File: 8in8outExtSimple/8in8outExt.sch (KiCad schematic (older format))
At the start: 70 parts, among them P1 CONN_10X2, Q1 PNP, Q10 NPN, Q11 NPN, Q12 NPN, Q13 NPN, Q14 NPN, Q15 NPN, Q16 NPN, Q2 PNP, Q3 PNP, Q4 PNP, Q5 PNP, Q6 PNP, Q7 PNP, Q8 PNP, Q9 NPN

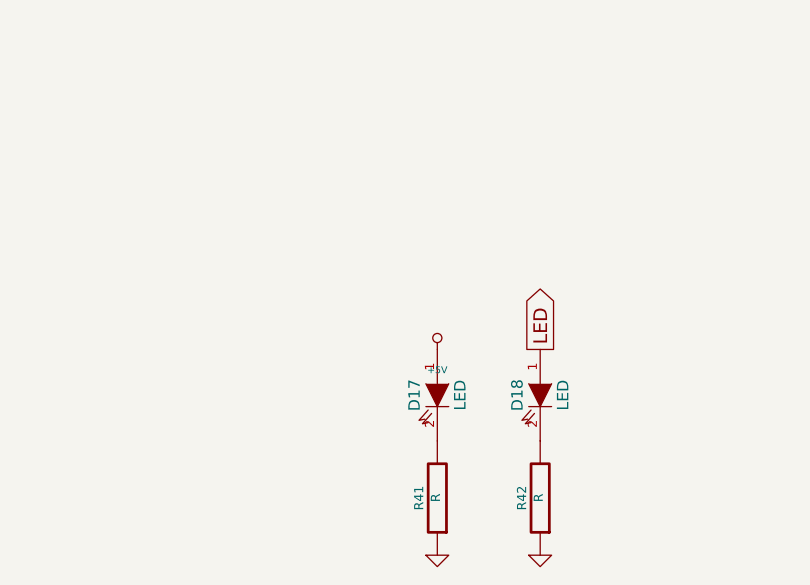
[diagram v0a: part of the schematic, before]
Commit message: agrandissement taille du panneau ajout NPN pour commande led status serigraphie
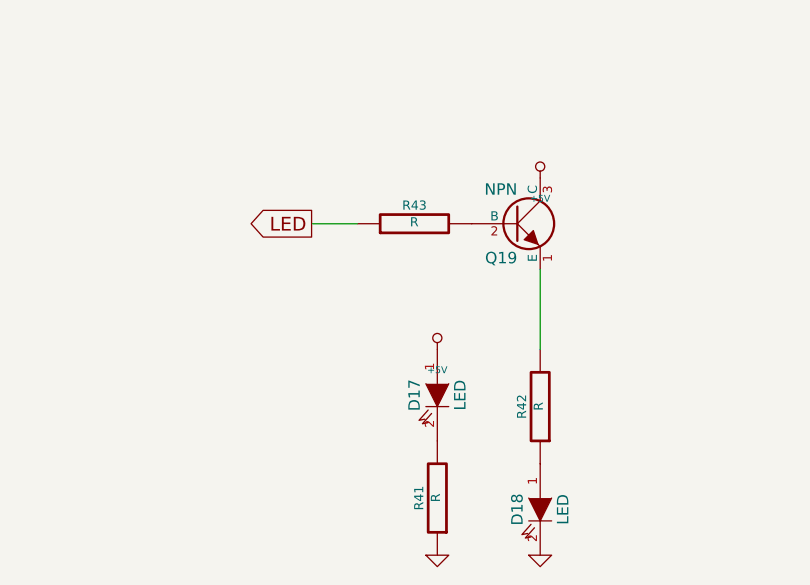
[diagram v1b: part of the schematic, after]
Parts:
- added Q19: NPN, symbol NPN
- added R43: R, symbol R
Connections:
- net +5V: now also Q19.3 (C)
- net GND: now also D18.2 (K); no longer R42.1
- net LED: now also R43.1; no longer D18.1 (A)
- net at R42.2: now also Q19.1 (E); no longer D18.2 (K)
- new net: D18.1 (A), R42.1
- new net: Q19.2 (B), R43.2
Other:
- moved on the sheet: D18, R42
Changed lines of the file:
@@
 L LED D18
 U 1 1 51739912
-P 12700 6750
-F 0 "D18" H 12700 6650 50  0000 C CNN
-F 1 "LED" H 12700 6850 50  0000 C CNN
-F 2 "~" H 12700 6750 60  0000 C CNN
-F 3 "~" H 12700 6750 60  0000 C CNN
-	1    12700 6750
+P 12700 7250
+F 0 "D18" H 12700 7150 50  0000 C CNN
+F 1 "LED" H 12700 7350 50  0000 C CNN
+F 2 "~" H 12700 7250 60  0000 C CNN
+F 3 "~" H 12700 7250 60  0000 C CNN
+	1    12700 7250
 	0    1    1    0
 $EndComp
@@
 L R R42
 U 1 1 51739918
-P 12700 7200
-F 0 "R42" V 12780 7200 40  0000 C CNN
-F 1 "R" V 12707 7199 40  0000 C CNN
-F 2 "~" V 12630 7200 30  0000 C CNN
-F 3 "~" H 12700 7200 30  0000 C CNN
-	1    12700 7200
+P 12700 6800
+F 0 "R42" V 12780 6800 40  0000 C CNN
+F 1 "R" V 12707 6799 40  0000 C CNN
+F 2 "~" V 12630 6800 30  0000 C CNN
+F 3 "~" H 12700 6800 30  0000 C CNN
+	1    12700 6800
 	-1   0    0    1
 $EndComp
@@
 	1    0    0    -1
 $EndComp
-Text GLabel 12700 6550 1    60   Output ~ 0
+Text GLabel 11700 6000 0    60   Output ~ 0
 LED
 $Comp
-L +5V #PWR015
+L +5V #PWR07
 U 1 1 51766852
 P 6200 800
-F 0 "#PWR015" H 6200 710 20  0001 C CNN
+F 0 "#PWR07" H 6200 710 20  0001 C CNN
 F 1 "+5V" H 6200 710 30  0000 C CNN
 F 2 "" H 6200 800 60  0000 C CNN
@@
 RESET
 $Comp
-L GND #PWR016
+L GND #PWR08
 U 1 1 517986C9
 P 14250 6800
-F 0 "#PWR016" H 14250 6800 30  0001 C CNN
+F 0 "#PWR08" H 14250 6800 30  0001 C CNN
 F 1 "GND" H 14250 6870 30  0001 C CNN
 F 2 "" H 14250 6800 60  0000 C CNN
@@
 $EndComp
 $Comp
-L GND #PWR017
+L GND #PWR09
 U 1 1 522CC8B0
 P 7150 2000
-F 0 "#PWR017" H 7150 2000 30  0001 C CNN
+F 0 "#PWR09" H 7150 2000 30  0001 C CNN
 F 1 "GND" H 7150 2070 30  0001 C CNN
 F 2 "" H 7150 2000 60  0000 C CNN
@@
 $EndComp
 $Comp
-L +5V #PWR018
+L +5V #PWR010
 U 1 1 522CC8B6
 P 6200 1450
-F 0 "#PWR018" H 6200 1360 20  0001 C CNN
+F 0 "#PWR010" H 6200 1360 20  0001 C CNN
 F 1 "+5V" H 6200 1360 30  0000 C CNN
 F 2 "" H 6200 1450 60  0000 C CNN
@@
 $EndComp
 $Comp
-L GND #PWR019
+L GND #PWR011
 U 1 1 522CC8D7
 P 7150 2650
-F 0 "#PWR019" H 7150 2650 30  0001 C CNN
+F 0 "#PWR011" H 7150 2650 30  0001 C CNN
 F 1 "GND" H 7150 2720 30  0001 C CNN
 F 2 "" H 7150 2650 60  0000 C CNN
@@
 $EndComp
 $Comp
-L +5V #PWR020
+L +5V #PWR012
 U 1 1 522CC8DD
 P 6200 2100
-F 0 "#PWR020" H 6200 2010 20  0001 C CNN
+F 0 "#PWR012" H 6200 2010 20  0001 C CNN
 F 1 "+5V" H 6200 2010 30  0000 C CNN
 F 2 "" H 6200 2100 60  0000 C CNN
@@
 $EndComp
 $Comp
-L GND #PWR021
+L GND #PWR013
 U 1 1 522CC908
 P 7150 3300
-F 0 "#PWR021" H 7150 3300 30  0001 C CNN
+F 0 "#PWR013" H 7150 3300 30  0001 C CNN
 F 1 "GND" H 7150 3370 30  0001 C CNN
 F 2 "" H 7150 3300 60  0000 C CNN
@@
 $EndComp
 $Comp
-L +5V #PWR022
+L +5V #PWR014
 U 1 1 522CC90E
 P 6200 2750
-F 0 "#PWR022" H 6200 2660 20  0001 C CNN
+F 0 "#PWR014" H 6200 2660 20  0001 C CNN
 F 1 "+5V" H 6200 2660 30  0000 C CNN
 F 2 "" H 6200 2750 60  0000 C CNN
@@
 $EndComp
 $Comp
-L GND #PWR023
+L GND #PWR015
 U 1 1 522CC930
 P 7150 4000
-F 0 "#PWR023" H 7150 4000 30  0001 C CNN
+F 0 "#PWR015" H 7150 4000 30  0001 C CNN
 F 1 "GND" H 7150 4070 30  0001 C CNN
 F 2 "" H 7150 4000 60  0000 C CNN
@@
 $EndComp
 $Comp
-L +5V #PWR024
+L +5V #PWR016
 U 1 1 522CC936
 P 6200 3450
-F 0 "#PWR024" H 6200 3360 20  0001 C CNN
+F 0 "#PWR016" H 6200 3360 20  0001 C CNN
 F 1 "+5V" H 6200 3360 30  0000 C CNN
 F 2 "" H 6200 3450 60  0000 C CNN
@@
 $EndComp
 $Comp
-L GND #PWR025
+L GND #PWR017
 U 1 1 522CC957
 P 7150 4650
-F 0 "#PWR025" H 7150 4650 30  0001 C CNN
+F 0 "#PWR017" H 7150 4650 30  0001 C CNN
 F 1 "GND" H 7150 4720 30  0001 C CNN
 F 2 "" H 7150 4650 60  0000 C CNN
@@
 $EndComp
 $Comp
-L +5V #PWR026
+L +5V #PWR018
 U 1 1 522CC95D
 P 6200 4100
-F 0 "#PWR026" H 6200 4010 20  0001 C CNN
+F 0 "#PWR018" H 6200 4010 20  0001 C CNN
 F 1 "+5V" H 6200 4010 30  0000 C CNN
 F 2 "" H 6200 4100 60  0000 C CNN
@@
 $EndComp
 $Comp
-L GND #PWR027
+L GND #PWR019
 U 1 1 522CC97E
 P 7150 5300
-F 0 "#PWR027" H 7150 5300 30  0001 C CNN
+F 0 "#PWR019" H 7150 5300 30  0001 C CNN
 F 1 "GND" H 7150 5370 30  0001 C CNN
 F 2 "" H 7150 5300 60  0000 C CNN
@@
 $EndComp
 $Comp
-L +5V #PWR028
+L +5V #PWR020
 U 1 1 522CC984
 P 6200 4750
-F 0 "#PWR028" H 6200 4660 20  0001 C CNN
+F 0 "#PWR020" H 6200 4660 20  0001 C CNN
 F 1 "+5V" H 6200 4660 30  0000 C CNN
 F 2 "" H 6200 4750 60  0000 C CNN
@@
 $EndComp
 $Comp
-L GND #PWR029
+L GND #PWR021
 U 1 1 522CC9A5
 P 7150 5950
-F 0 "#PWR029" H 7150 5950 30  0001 C CNN
+F 0 "#PWR021" H 7150 5950 30  0001 C CNN
 F 1 "GND" H 7150 6020 30  0001 C CNN
 F 2 "" H 7150 5950 60  0000 C CNN
@@
 $EndComp
 $Comp
-L +5V #PWR030
+L +5V #PWR022
 U 1 1 522CC9AB
 P 6200 5400
-F 0 "#PWR030" H 6200 5310 20  0001 C CNN
+F 0 "#PWR022" H 6200 5310 20  0001 C CNN
 F 1 "+5V" H 6200 5310 30  0000 C CNN
 F 2 "" H 6200 5400 60  0000 C CNN
@@
 $EndComp
 $Comp
-L GND #PWR031
+L GND #PWR023
 U 1 1 522CC9E4
 P 9800 1350
-F 0 "#PWR031" H 9800 1350 30  0001 C CNN
+F 0 "#PWR023" H 9800 1350 30  0001 C CNN
 F 1 "GND" H 9800 1420 30  0001 C CNN
 F 2 "" H 9800 1350 60  0000 C CNN
@@
 $EndComp
 $Comp
-L +5V #PWR032
+L +5V #PWR024
 U 1 1 522CC9EA
 P 8850 800
-F 0 "#PWR032" H 8850 710 20  0001 C CNN
+F 0 "#PWR024" H 8850 710 20  0001 C CNN
 F 1 "+5V" H 8850 710 30  0000 C CNN
 F 2 "" H 8850 800 60  0000 C CNN
@@
 $EndComp
 $Comp
-L GND #PWR033
+L GND #PWR025
 U 1 1 522CCA2C
 P 9800 2000
-F 0 "#PWR033" H 9800 2000 30  0001 C CNN
+F 0 "#PWR025" H 9800 2000 30  0001 C CNN
 F 1 "GND" H 9800 2070 30  0001 C CNN
 F 2 "" H 9800 2000 60  0000 C CNN
@@
 $EndComp
 $Comp
-L +5V #PWR034
+L +5V #PWR026
 U 1 1 522CCA32
 P 8850 1450
-F 0 "#PWR034" H 8850 1360 20  0001 C CNN
+F 0 "#PWR026" H 8850 1360 20  0001 C CNN
 F 1 "+5V" H 8850 1360 30  0000 C CNN
 F 2 "" H 8850 1450 60  0000 C CNN
@@
 $EndComp
 $Comp
-L GND #PWR035
+L GND #PWR027
 U 1 1 522CCA53
 P 9800 2650
-F 0 "#PWR035" H 9800 2650 30  0001 C CNN
+F 0 "#PWR027" H 9800 2650 30  0001 C CNN
 F 1 "GND" H 9800 2720 30  0001 C CNN
 F 2 "" H 9800 2650 60  0000 C CNN
@@
 $EndComp
 $Comp
-L +5V #PWR036
+L +5V #PWR028
 U 1 1 522CCA59
 P 8850 2100
-F 0 "#PWR036" H 8850 2010 20  0001 C CNN
+F 0 "#PWR028" H 8850 2010 20  0001 C CNN
 F 1 "+5V" H 8850 2010 30  0000 C CNN
 F 2 "" H 8850 2100 60  0000 C CNN
@@
 $EndComp
 $Comp
-L GND #PWR037
+L GND #PWR029
 U 1 1 522CCA7A
 P 9800 3300
-F 0 "#PWR037" H 9800 3300 30  0001 C CNN
+F 0 "#PWR029" H 9800 3300 30  0001 C CNN
 F 1 "GND" H 9800 3370 30  0001 C CNN
 F 2 "" H 9800 3300 60  0000 C CNN
@@
 $EndComp
 $Comp
-L +5V #PWR038
+L +5V #PWR030
 U 1 1 522CCA80
 P 8850 2750
-F 0 "#PWR038" H 8850 2660 20  0001 C CNN
+F 0 "#PWR030" H 8850 2660 20  0001 C CNN
 F 1 "+5V" H 8850 2660 30  0000 C CNN
 F 2 "" H 8850 2750 60  0000 C CNN
@@
 $EndComp
 $Comp
-L GND #PWR039
+L GND #PWR031
 U 1 1 522CCAA1
 P 9800 4000
-F 0 "#PWR039" H 9800 4000 30  0001 C CNN
+F 0 "#PWR031" H 9800 4000 30  0001 C CNN
 F 1 "GND" H 9800 4070 30  0001 C CNN
 F 2 "" H 9800 4000 60  0000 C CNN
@@
 $EndComp
 $Comp
-L +5V #PWR040
+L +5V #PWR032
 U 1 1 522CCAA7
 P 8850 3450
-F 0 "#PWR040" H 8850 3360 20  0001 C CNN
+F 0 "#PWR032" H 8850 3360 20  0001 C CNN
 F 1 "+5V" H 8850 3360 30  0000 C CNN
 F 2 "" H 8850 3450 60  0000 C CNN
@@
 $EndComp
 $Comp
-L GND #PWR041
+L GND #PWR033
 U 1 1 522CCAC8
 P 9850 4650
-F 0 "#PWR041" H 9850 4650 30  0001 C CNN
+F 0 "#PWR033" H 9850 4650 30  0001 C CNN
 F 1 "GND" H 9850 4720 30  0001 C CNN
 F 2 "" H 9850 4650 60  0000 C CNN
@@
 $EndComp
 $Comp
-L +5V #PWR042
+L +5V #PWR034
 U 1 1 522CCACE
 P 8850 4100
-F 0 "#PWR042" H 8850 4010 20  0001 C CNN
+F 0 "#PWR034" H 8850 4010 20  0001 C CNN
 F 1 "+5V" H 8850 4010 30  0000 C CNN
 F 2 "" H 8850 4100 60  0000 C CNN
@@
 $EndComp
 $Comp
-L GND #PWR043
+L GND #PWR035
 U 1 1 522CCAEF
 P 9800 5300
-F 0 "#PWR043" H 9800 5300 30  0001 C CNN
+F 0 "#PWR035" H 9800 5300 30  0001 C CNN
 F 1 "GND" H 9800 5370 30  0001 C CNN
 F 2 "" H 9800 5300 60  0000 C CNN
@@
 $EndComp
 $Comp
-L +5V #PWR044
+L +5V #PWR036
 U 1 1 522CCAF5
 P 8850 4750
-F 0 "#PWR044" H 8850 4660 20  0001 C CNN
+F 0 "#PWR036" H 8850 4660 20  0001 C CNN
 F 1 "+5V" H 8850 4660 30  0000 C CNN
 F 2 "" H 8850 4750 60  0000 C CNN
@@
 $EndComp
 $Comp
-L GND #PWR045
+L GND #PWR037
 U 1 1 522CCB16
 P 9800 5950
-F 0 "#PWR045" H 9800 5950 30  0001 C CNN
+F 0 "#PWR037" H 9800 5950 30  0001 C CNN
 F 1 "GND" H 9800 6020 30  0001 C CNN
 F 2 "" H 9800 5950 60  0000 C CNN
@@
 $EndComp
 $Comp
-L +5V #PWR046
+L +5V #PWR038
 U 1 1 522CCB1C
 P 8850 5400
-F 0 "#PWR046" H 8850 5310 20  0001 C CNN
+F 0 "#PWR038" H 8850 5310 20  0001 C CNN
 F 1 "+5V" H 8850 5310 30  0000 C CNN
 F 2 "" H 8850 5400 60  0000 C CNN
@@
 	1    0    0    -1
 $EndComp
+Wire Wire Line
+	11700 6000 11900 6000
+$Comp
+L +5V #PWR039
+U 1 1 52681A86
+P 12700 5800
+F 0 "#PWR039" H 12700 5710 20  0001 C CNN
+F 1 "+5V" H 12700 5710 30  0000 C CNN
+F 2 "" H 12700 5800 60  0000 C CNN
+F 3 "" H 12700 5800 60  0000 C CNN
+	1    12700 5800
+	1    0    0    -1
+$EndComp
+$Comp
+L R R43
+U 1 1 52681A8C
+P 12150 6000
+F 0 "R43" V 12230 6000 40  0000 C CNN
+F 1 "R" V 12157 6001 40  0000 C CNN
+F 2 "" V 12080 6000 30  0000 C CNN
+F 3 "" H 12150 6000 30  0000 C CNN
+	1    12150 6000
+	0    -1   -1   0
+$EndComp
+$Comp
+L NPN Q19
+U 1 1 52681A92
+P 12600 6000
+F 0 "Q19" H 12600 5850 50  0000 R CNN
+F 1 "NPN" H 12600 6150 50  0000 R CNN
+F 2 "" H 12600 6000 60  0000 C CNN
+F 3 "" H 12600 6000 60  0000 C CNN
+	1    12600 6000
+	1    0    0    -1
+$EndComp
+Wire Wire Line
+	12700 6550 12700 6200
 $EndSCHEMATC

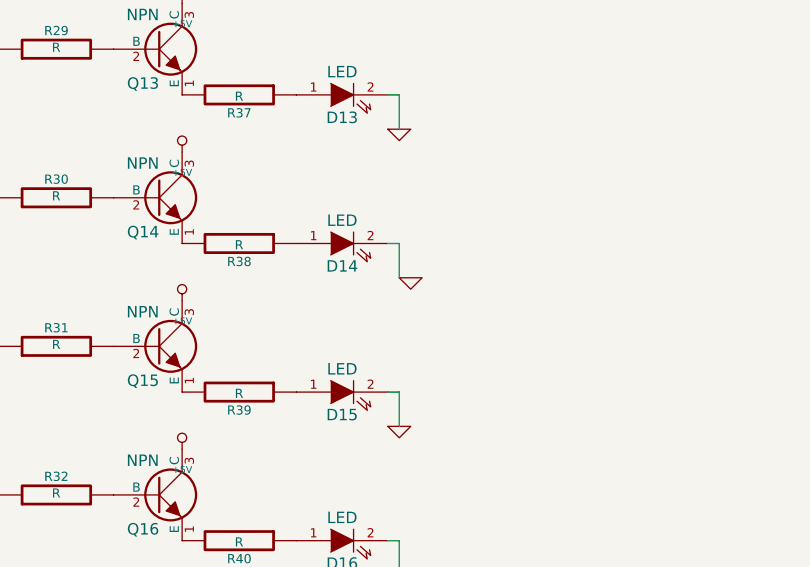
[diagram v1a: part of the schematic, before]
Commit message: correction erreur schema led out5 pas reli? au GND
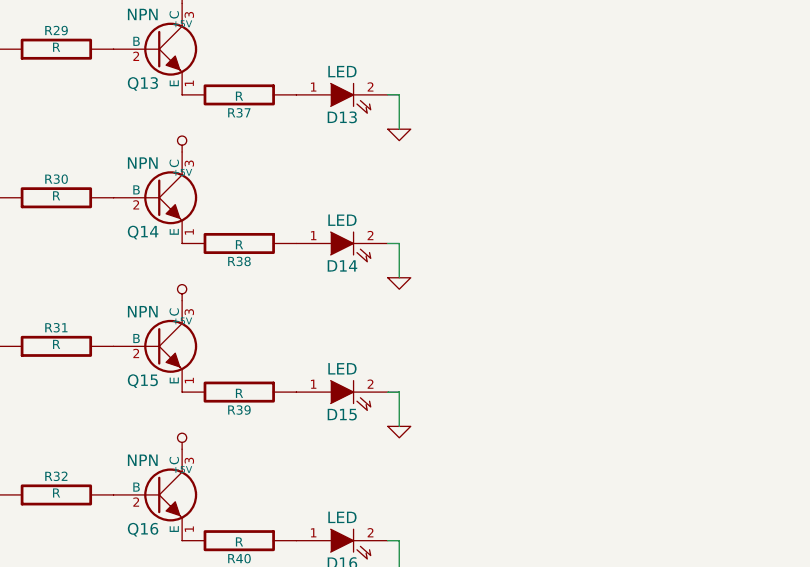
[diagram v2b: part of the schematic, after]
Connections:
- net GND: now also D14.2 (K)
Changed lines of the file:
@@
 L GND #PWR033
 U 1 1 522CCAC8
-P 9850 4650
-F 0 "#PWR033" H 9850 4650 30  0001 C CNN
-F 1 "GND" H 9850 4720 30  0001 C CNN
-F 2 "" H 9850 4650 60  0000 C CNN
-F 3 "" H 9850 4650 60  0000 C CNN
-	1    9850 4650
+P 9800 4650
+F 0 "#PWR033" H 9800 4650 30  0001 C CNN
+F 1 "GND" H 9800 4720 30  0001 C CNN
+F 2 "" H 9800 4650 60  0000 C CNN
+F 3 "" H 9800 4650 60  0000 C CNN
+	1    9800 4650
 	1    0    0    -1
 $EndComp
